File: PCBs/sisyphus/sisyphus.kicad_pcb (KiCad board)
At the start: 2 copper layers, 51.5 x 36.5 mm, 65 parts, among them J1 Battery, J2 USB_C_Receptacle_USB2.0_14P, J3 USB_BOOT, J4 SPK, J5 RGB_CONN, J6 AUX, J7 SWD, J8 KEYB, J9 PWR-BTN, Q1 AO3401A, SW1 SW_SPDT_321, U1 TPS62291, U2 MP2667, U3 USBLC6-2P6, U4 MAX17048, U5 W25Q128JVP, U6 TCA8418, U7 MAX98357A, U8 RP2040, Y1 ABM8-272-T3

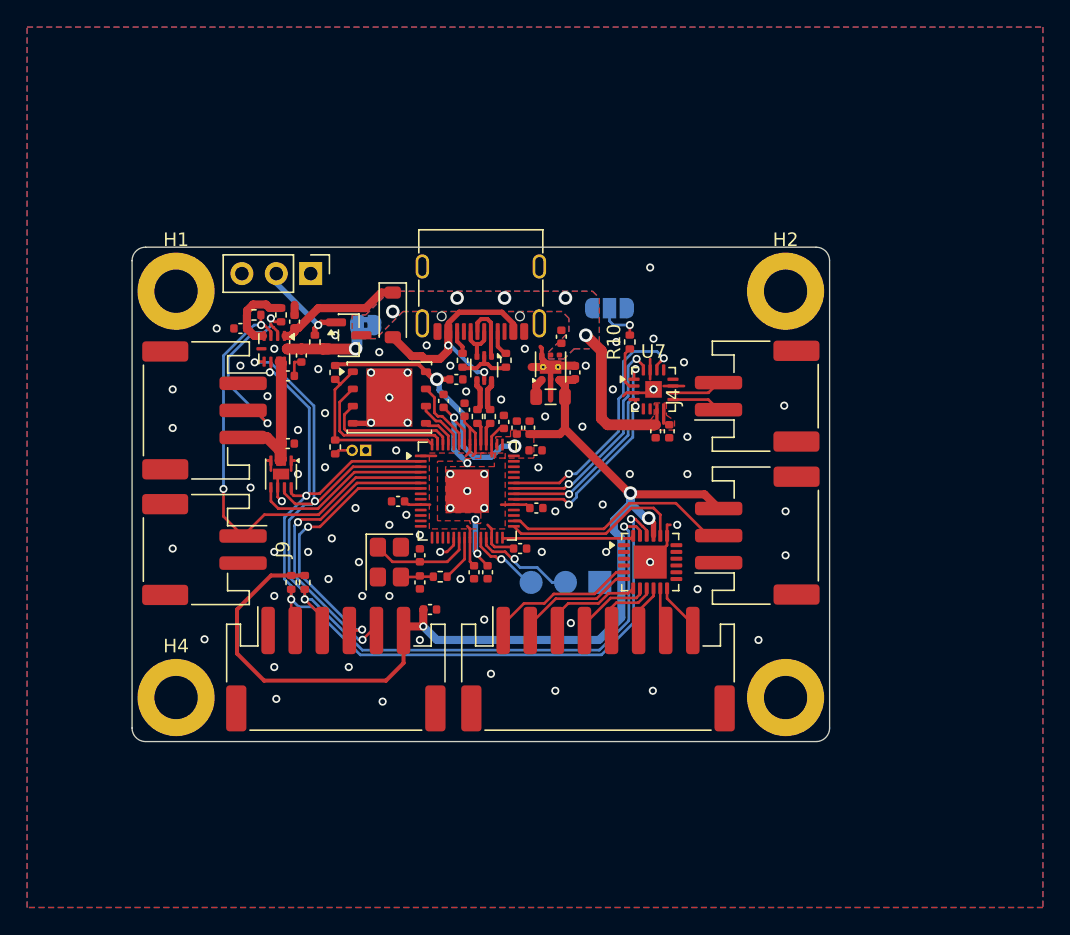
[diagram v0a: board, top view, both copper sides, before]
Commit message: Remove unwanted 3D models, move SWD
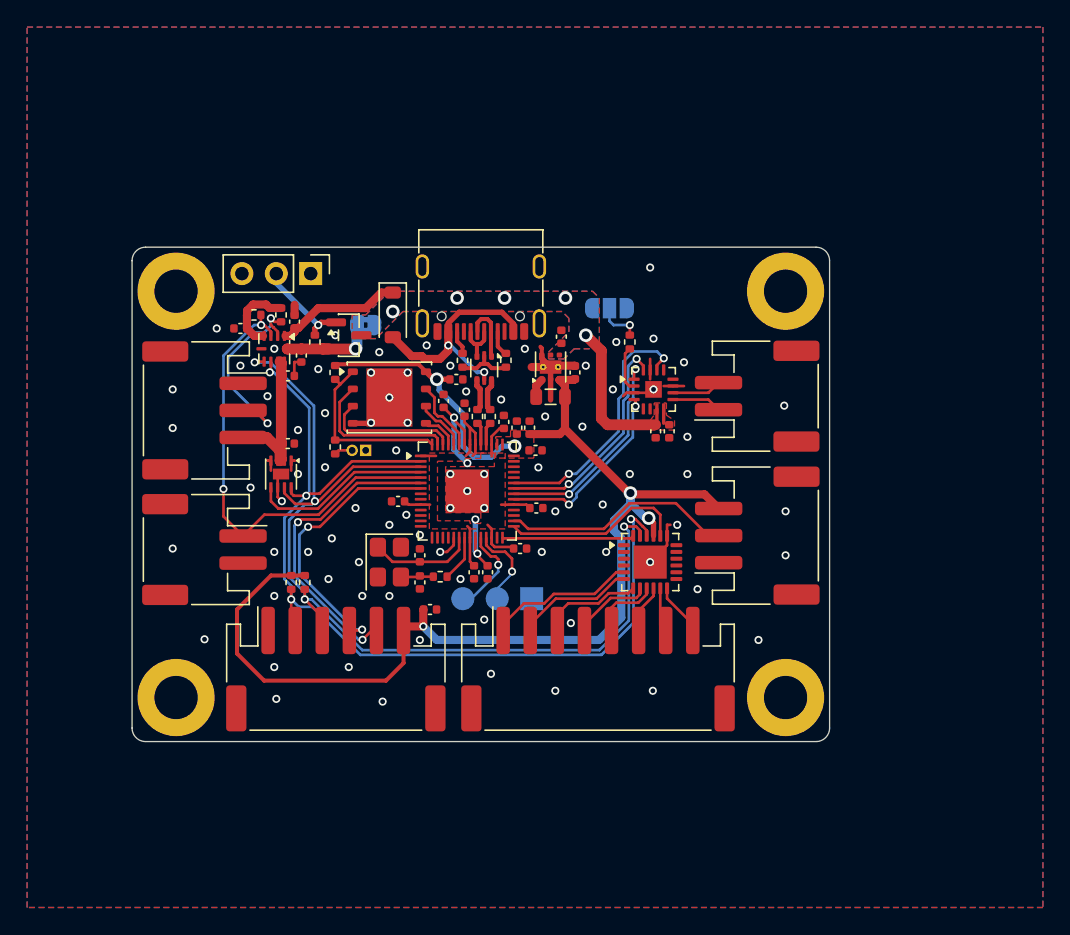
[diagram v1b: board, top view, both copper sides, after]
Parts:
- moved J7 5.18 mm to (107.2, 101.2)
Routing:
- net /SWD: track 7.69 -> 6.28 mm
- net /SWCLK: track 5.46 -> 6.69 mm
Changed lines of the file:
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@@
 			(psnegative no)
 			(psa4output no)
-			(plot_black_and_white yes)
+			(plot_black_and_white no)
 			(sketchpadsonfab no)
 			(plotpadnumbers no)
@@
 			(at 0 -3.8 0)
 			(layer "F.SilkS")
+			(hide yes)
 			(effects
 				(font
@@
 			(at 0 -3.8 0)
 			(layer "F.SilkS")
+			(hide yes)
 			(effects
 				(font
@@
 			(at 0 -5.8 90)
 			(layer "F.SilkS")
+			(hide yes)
 			(effects
 				(font
@@
 			(at -0.05 -6.2 90)
 			(layer "F.SilkS")
+			(hide yes)
 			(effects
 				(font
@@
 		(embedded_fonts no)
 		(model "${KICAD10_3DMODEL_DIR}/Connector_PinHeader_1.00mm.3dshapes/PinHeader_1x02_P1.00mm_Vertical.step"
+			(hide yes)
 			(offset
 				(xyz 0 0 0)
@@
 			(at 0 -1.17 90)
 			(layer "F.SilkS")
+			(hide yes)
 			(effects
 				(font
@@
 			(at 0 -2.8 0)
 			(layer "F.SilkS")
+			(hide yes)
 			(effects
 				(font
@@
 		(embedded_fonts no)
 		(model "${KICAD10_3DMODEL_DIR}/Connector_PinHeader_2.54mm.3dshapes/PinHeader_1x03_P2.54mm_Vertical.step"
+			(hide yes)
 			(offset
 				(xyz 0 0 0)
@@
 			(at 0 -3.8 0)
 			(layer "F.SilkS")
+			(hide yes)
 			(effects
 				(font
@@
 	(footprint "Connector_PinHeader_2.54mm:PinHeader_1x03_P2.54mm_Vertical"
 		(layer "B.Cu")
-		(at 112.29 100 90)
+		(at 107.25 101.2 90)
 		(descr "Through hole straight pin header, 1x03, 2.54mm pitch, single row")
 		(tags "Through hole pin header THT 1x03 2.54mm single row")
@@
 		(sheetname "/")
 		(sheetfile "sisyphus.kicad_sch")
-		(units
-			(unit
-				(name "A")
-				(pins "1" "2" "3")
-			)
-		)
 		(attr through_hole exclude_from_bom dnp)
 		(duplicate_pad_numbers_are_jumpers no)
 		(fp_line
-			(start -1.38 -6.46)
-			(end 1.38 -6.46)
-			(stroke
-				(width 0.12)
-				(type solid)
-			)
-			(layer "B.SilkS")
-		)
-		(fp_line
-			(start 1.38 -1.27)
-			(end 1.38 -6.46)
-			(stroke
-				(width 0.12)
-				(type solid)
-			)
-			(layer "B.SilkS")
-		)
-		(fp_line
-			(start -1.38 -1.27)
-			(end -1.38 -6.46)
-			(stroke
-				(width 0.12)
-				(type solid)
-			)
-			(layer "B.SilkS")
-		)
-		(fp_line
-			(start -1.38 -1.27)
-			(end 1.38 -1.27)
-			(stroke
-				(width 0.12)
-				(type solid)
-			)
-			(layer "B.SilkS")
-		)
-		(fp_line
 			(start -1.38 0)
 			(end -1.38 1.38)
@@
 		(embedded_fonts no)
 		(model "${KICAD10_3DMODEL_DIR}/Connector_PinHeader_2.54mm.3dshapes/PinHeader_1x03_P2.54mm_Vertical.step"
+			(hide yes)
 			(offset
 				(xyz 0 0 0)
@@
 	)
 	(segment
+		(start 104.785 98.7)
+		(end 104.785 98.285)
+		(width 0.2)
+		(layer "F.Cu")
+		(net "/SWCLK")
+	)
+	(segment
 		(start 104.234401 98.085)
 		(end 103.5 97.350598)
@@
 	)
 	(segment
-		(start 105.013379 98.285)
-		(end 104.785 98.285)
+		(start 104.585 98.085)
+		(end 104.234401 98.085)
 		(width 0.2)
 		(layer "F.Cu")
@@
 		(net "/SWCLK")
 	)
-	(segment
-		(start 104.585 98.085)
-		(end 104.234401 98.085)
-		(width 0.2)
-		(layer "F.Cu")
-		(net "/SWCLK")
-	)
 	(via
-		(at 105.013379 98.285)
+		(at 104.785 98.7)
 		(size 0.6)
 		(drill 0.35)
@@
 	)
 	(segment
-		(start 105.013379 98.285)
-		(end 105.246544 98.285)
+		(start 104.785 99.215)
+		(end 102.8 101.2)
 		(width 0.2)
 		(layer "B.Cu")
@@
 	)
 	(segment
-		(start 106.961544 100)
-		(end 107.21 100)
+		(start 102.8 101.2)
+		(end 102.17 101.2)
 		(width 0.2)
 		(layer "B.Cu")
@@
 	)
 	(segment
-		(start 105.246544 98.285)
-		(end 106.961544 100)
+		(start 104.785 98.7)
+		(end 104.785 99.215)
 		(width 0.2)
 		(layer "B.Cu")
@@
 	)
 	(segment
-		(start 105.804576 98.25)
-		(end 105.289576 97.735)
-		(width 0.2)
-		(layer "F.Cu")
-		(net "/SWD")
-	)
-	(segment
-		(start 105.999362 98.26)
-		(end 105.989362 98.25)
+		(start 103.9 97.255624)
+		(end 103.9 96.6975)
 		(width 0.2)
 		(layer "F.Cu")
@@
 	)
 	(segment
-		(start 105.989362 98.25)
-		(end 105.804576 98.25)
+		(start 105.289576 97.735)
+		(end 104.379376 97.735)
 		(width 0.2)
 		(layer "F.Cu")
@@
 	)
 	(segment
-		(start 104.379376 97.735)
-		(end 103.9 97.255624)
+		(start 105.804576 98.25)
+		(end 105.289576 97.735)
 		(width 0.2)
 		(layer "F.Cu")
@@
 	)
 	(segment
-		(start 105.289576 97.735)
-		(end 104.379376 97.735)
+		(start 105.804576 99.2)
+		(end 105.804576 98.25)
 		(width 0.2)
 		(layer "F.Cu")
@@
 	)
 	(segment
-		(start 103.9 97.255624)
-		(end 103.9 96.6975)
+		(start 104.379376 97.735)
+		(end 103.9 97.255624)
 		(width 0.2)
 		(layer "F.Cu")
@@
 	)
 	(via
-		(at 105.999362 98.26)
+		(at 105.804576 99.2)
 		(size 0.6)
 		(drill 0.35)
@@
 	)
 	(segment
-		(start 105.999362 98.26)
-		(end 105.999362 98.499362)
-		(width 0.2)
+		(start 104.81 101)
+		(end 104.81 100.35)
+		(width 0.15)
 		(layer "B.Cu")
 		(net "/SWD")
 	)
 	(segment
-		(start 105.999362 98.499362)
-		(end 106.4 98.9)
-		(width 0.2)
+		(start 104.71 101.1)
+		(end 104.81 101)
+		(width 0.15)
 		(layer "B.Cu")
 		(net "/SWD")
 	)
 	(segment
-		(start 108.765635 100)
-		(end 109.75 100)
+		(start 105.804576 99.2)
+		(end 105.8 99.204576)
 		(width 0.2)
 		(layer "B.Cu")
@@
 	)
 	(segment
-		(start 106.4 98.9)
-		(end 107.665635 98.9)
-		(width 0.2)
+		(start 104.71 101.2)
+		(end 104.71 101.1)
+		(width 0.15)
 		(layer "B.Cu")
 		(net "/SWD")
 	)
 	(segment
-		(start 107.665635 98.9)
-		(end 108.765635 100)
-		(width 0.2)
+		(start 105.804576 99.355424)
+		(end 105.804576 99.2)
+		(width 0.15)
+		(layer "B.Cu")
+		(net "/SWD")
+	)
+	(segment
+		(start 104.81 100.35)
+		(end 105.804576 99.355424)
+		(width 0.15)
 		(layer "B.Cu")
 		(net "/SWD")
